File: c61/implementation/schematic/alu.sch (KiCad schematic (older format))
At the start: 22 parts, among them J4 CONN_02X05, U1 74LS32, U2 74LS32, U3 74LVC1G99, U30 EPM3064ATC44-ALU6, U4 74LVC1G99, U5 74LVC1G99, U6 74LVC1G99, U7 74LVC1G99, U8 74LVC1G99

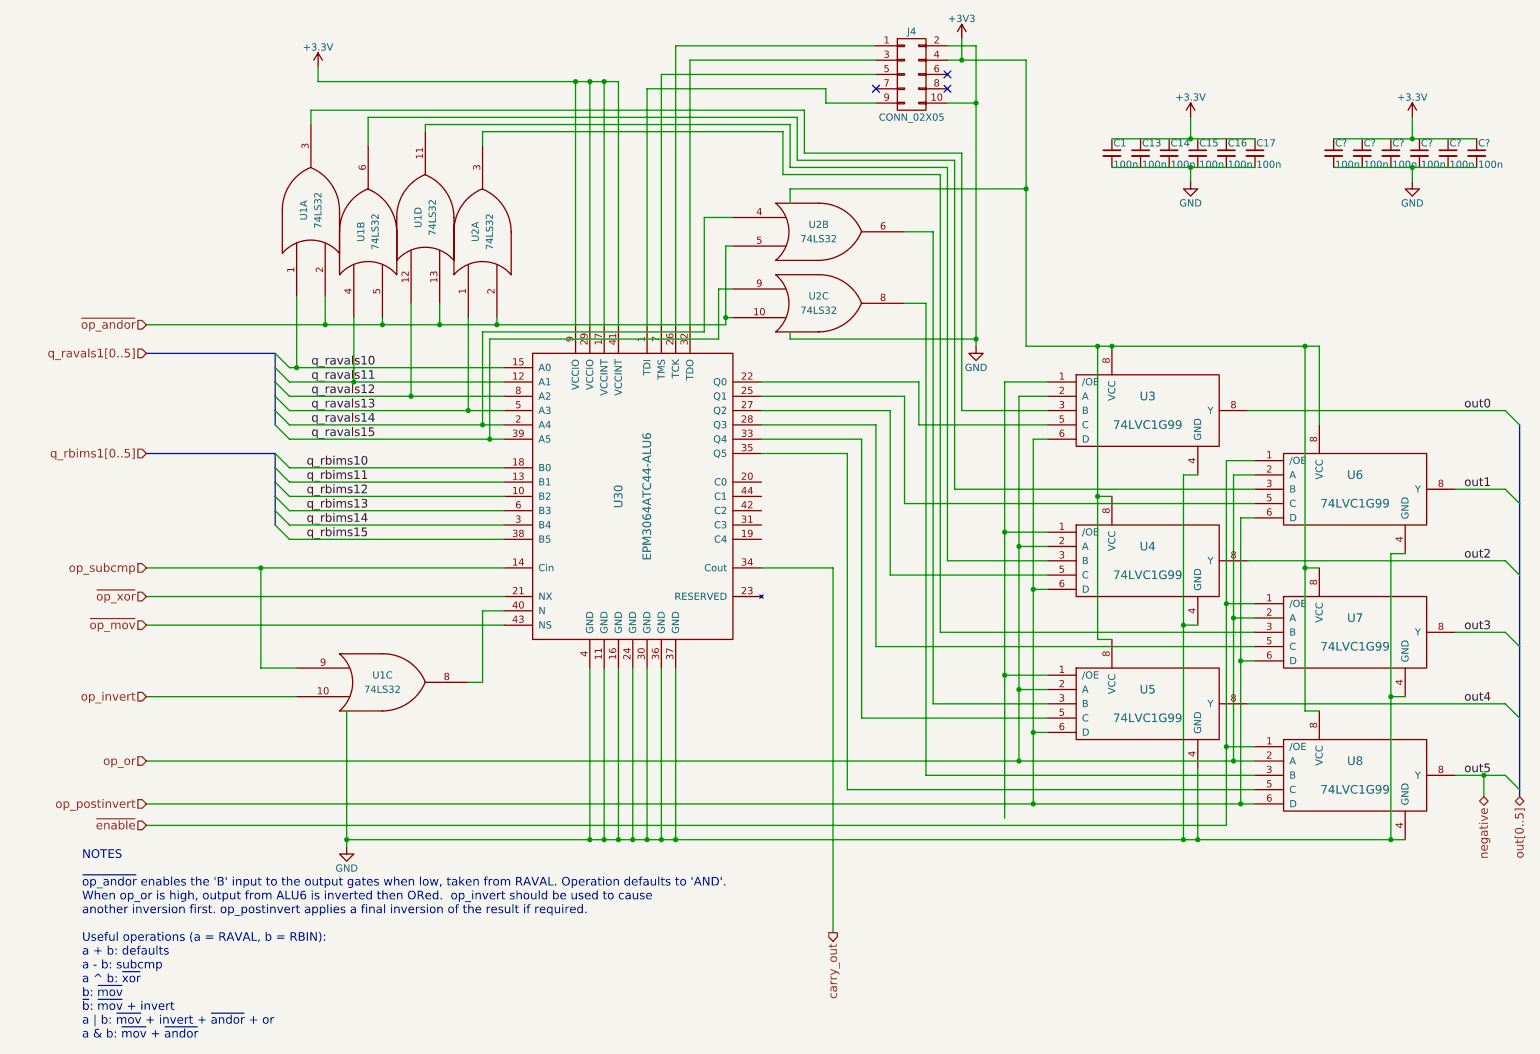
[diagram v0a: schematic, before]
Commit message: C61: more updates to schematic
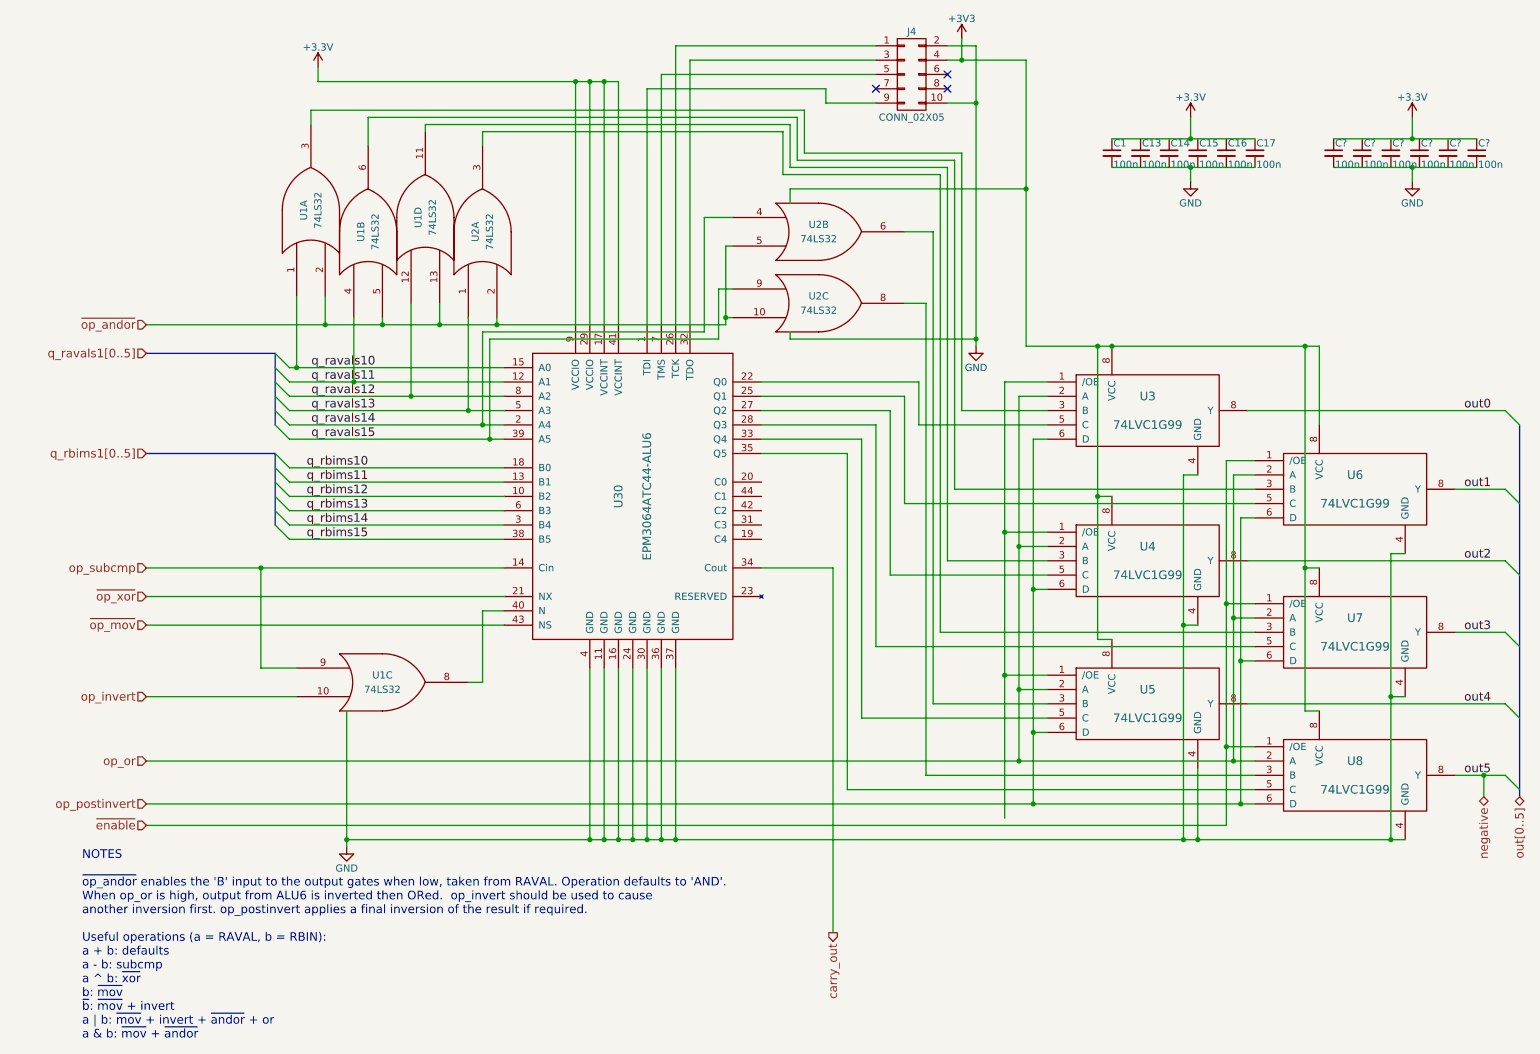
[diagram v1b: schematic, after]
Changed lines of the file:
@@
 $Descr A4 11693 8268
 encoding utf-8
-Sheet 7 8
+Sheet 7 9
 Title ""
 Date ""
@@
 	1400 3650 2300 3650
 Wire Bus Line
-	2300 3650 2300 3750
-Wire Bus Line
-	2300 3750 2300 3850
-Wire Bus Line
-	2300 3850 2300 3950
-Wire Bus Line
-	2300 3950 2300 4050
-Wire Bus Line
-	2300 4050 2300 4150
+	2300 3650 2300 4150
 Wire Wire Line
 	2400 3750 3900 3750
@@
 	1400 2950 2300 2950
 Wire Bus Line
-	2300 2950 2300 3050
-Wire Bus Line
-	2300 3050 2300 3150
-Wire Bus Line
-	2300 3150 2300 3250
-Wire Bus Line
-	2300 3250 2300 3350
-Wire Bus Line
-	2300 3350 2300 3450
-Wire Wire Line
-	2400 3050 2450 3050
-Wire Wire Line
-	2450 3050 3900 3050
-Wire Wire Line
-	2400 3150 2850 3150
-Wire Wire Line
-	2850 3150 3900 3150
-Wire Wire Line
-	2400 3250 3250 3250
-Wire Wire Line
-	3250 3250 3900 3250
-Wire Wire Line
-	2400 3350 3650 3350
-Wire Wire Line
-	3650 3350 3900 3350
-Wire Wire Line
-	2400 3450 3750 3450
-Wire Wire Line
-	3750 3450 3900 3450
-Wire Wire Line
-	2400 3550 3800 3550
-Wire Wire Line
-	3800 3550 3900 3550
-Wire Wire Line
-	1400 4450 2200 4450
-Wire Wire Line
-	2200 4450 3900 4450
+	2300 2950 2300 3450
+Wire Wire Line
+	2400 3050 3900 3050
+Wire Wire Line
+	2400 3150 3900 3150
+Wire Wire Line
+	2400 3250 3900 3250
+Wire Wire Line
+	2400 3350 3900 3350
+Wire Wire Line
+	2400 3450 3900 3450
+Wire Wire Line
+	2400 3550 3900 3550
+Wire Wire Line
+	1400 4450 3900 4450
 Wire Wire Line
 	1400 4650 3900 4650
@@
 	1400 5350 2450 5350
 Wire Wire Line
-	2800 5450 2800 6350
-Wire Wire Line
-	2800 6350 2800 6400
-Wire Wire Line
-	2800 6350 4500 6350
-Wire Wire Line
-	4500 6350 4600 6350
-Wire Wire Line
-	4600 6350 4700 6350
-Wire Wire Line
-	4700 6350 4800 6350
-Wire Wire Line
-	4800 6350 4900 6350
-Wire Wire Line
-	4900 6350 5000 6350
-Wire Wire Line
-	5000 6350 5100 6350
-Wire Wire Line
-	5100 6350 8650 6350
-Wire Wire Line
-	8650 6350 8750 6350
-Wire Wire Line
-	8750 6350 10100 6350
-Wire Wire Line
-	10100 6350 10200 6350
+	2800 5450 2800 6400
+Wire Wire Line
+	2800 6350 10200 6350
 Wire Wire Line
 	5100 6350 5100 5150
@@
 	2600 950  2600 1050
 Wire Wire Line
-	2600 1050 4400 1050
-Wire Wire Line
-	4400 1050 4500 1050
-Wire Wire Line
-	4500 1050 4600 1050
-Wire Wire Line
-	4600 1050 4700 1050
+	2600 1050 4700 1050
 Wire Wire Line
 	4700 1050 4700 2750
@@
 	7000 800  7200 800
 Wire Wire Line
-	7200 800  7200 1200
-Wire Wire Line
-	7200 1200 7200 2850
-Wire Wire Line
-	7200 2850 7200 2900
+	7200 800  7200 2900
 Wire Wire Line
 	7000 1200 7200 1200
 Connection ~ 7200 1200
 Wire Wire Line
-	7000 900  7100 900
-Wire Wire Line
-	7100 900  7550 900
+	7000 900  7550 900
 Wire Wire Line
 	7100 900  7100 750
@@
 	8700 1300 8700 1450
 Wire Wire Line
-	8150 1450 8700 1450
-Wire Wire Line
-	8700 1450 9150 1450
+	8150 1450 9150 1450
 Connection ~ 8700 1450
 Wire Wire Line
-	8150 1650 8700 1650
-Wire Wire Line
-	8700 1650 9150 1650
+	8150 1650 9150 1650
 Wire Wire Line
 	8700 1650 8700 1750
@@
 Connection ~ 2450 3050
 Wire Wire Line
-	5450 2750 3850 2750
-Wire Wire Line
-	3850 2750 3450 2750
-Wire Wire Line
-	3450 2750 3050 2750
-Wire Wire Line
-	3050 2750 2650 2750
-Wire Wire Line
-	2650 2750 1400 2750
+	5450 2750 1400 2750
 Wire Wire Line
 	2650 2550 2650 2750
@@
 Connection ~ 3450 2750
 Wire Wire Line
-	5450 2200 5450 2700
-Wire Wire Line
-	5450 2700 5450 2750
+	5450 2200 5450 2750
 Wire Wire Line
 	5450 2700 5500 2700
@@
 Connection ~ 2200 4450
 Wire Wire Line
-	1400 6100 7600 6100
-Wire Wire Line
-	7600 6100 9050 6100
-Wire Wire Line
-	9050 6100 9150 6100
-Wire Wire Line
-	9050 4100 9050 5100
-Wire Wire Line
-	9050 5100 9050 6100
+	1400 6100 9150 6100
+Wire Wire Line
+	9050 4100 9050 6100
 Wire Wire Line
 	9050 5100 9150 5100
@@
 Connection ~ 9050 5100
 Wire Wire Line
-	7600 3550 7600 4600
-Wire Wire Line
-	7600 4600 7600 5600
-Wire Wire Line
-	7600 5600 7600 6100
+	7600 3550 7600 6100
 Wire Wire Line
 	7600 5600 7700 5600
@@
 Connection ~ 7600 4600
 Wire Wire Line
-	1400 5800 7500 5800
-Wire Wire Line
-	7500 5800 9000 5800
-Wire Wire Line
-	9000 5800 9150 5800
-Wire Wire Line
-	7500 3250 7500 4300
-Wire Wire Line
-	7500 4300 7500 5300
-Wire Wire Line
-	7500 5300 7500 5800
+	1400 5800 9150 5800
+Wire Wire Line
+	7500 3250 7500 5800
 Wire Wire Line
 	7500 5300 7700 5300
@@
 Connection ~ 7500 4300
 Wire Wire Line
-	9000 3800 9000 4800
-Wire Wire Line
-	9000 4800 9000 5800
+	9000 3800 9000 5800
 Wire Wire Line
 	9000 4800 9150 4800
@@
 	8950 5700 9150 5700
 Wire Wire Line
-	8950 3700 8950 4700
-Wire Wire Line
-	8950 4700 8950 5700
-Wire Wire Line
-	8950 5700 8950 6250
+	8950 3700 8950 6250
 Wire Wire Line
 	8950 6250 1400 6250
@@
 Connection ~ 8950 4700
 Wire Wire Line
-	7400 3150 7400 4200
-Wire Wire Line
-	7400 4200 7400 5200
-Wire Wire Line
-	7400 5200 7400 6200
+	7400 3150 7400 6200
 Wire Wire Line
 	7400 5200 7700 5200
@@
 Connection ~ 8750 6350
 Wire Wire Line
-	10100 4350 10100 5350
-Wire Wire Line
-	10100 5350 10100 6350
+	10100 4350 10100 6350
 Wire Wire Line
 	10100 5350 10200 5350
@@
 Connection ~ 10100 5350
 Wire Wire Line
-	8650 3800 8650 4850
-Wire Wire Line
-	8650 4850 8650 6350
+	8650 3800 8650 6350
 Wire Wire Line
 	8650 4850 8750 4850
@@
 Connection ~ 8650 4850
 Wire Wire Line
-	7550 900  7550 1800
-Wire Wire Line
-	7550 1800 7550 2900
-Wire Wire Line
-	7550 2900 8050 2900
-Wire Wire Line
-	8050 2900 8150 2900
-Wire Wire Line
-	8150 2900 9500 2900
-Wire Wire Line
-	9500 2900 9600 2900
+	7550 900  7550 2900
+Wire Wire Line
+	7550 2900 9600 2900
 Connection ~ 7100 900
 Wire Wire Line
-	8050 2900 8050 3950
-Wire Wire Line
-	8050 3950 8050 4950
+	8050 2900 8050 4950
 Wire Wire Line
 	8050 3950 8150 3950
@@
 Connection ~ 8150 2900
 Wire Wire Line
-	9500 2900 9500 4450
-Wire Wire Line
-	9500 4450 9500 5450
+	9500 2900 9500 5450
 Wire Wire Line
 	9500 4450 9600 4450
@@
 	10900 5900 11000 6000
 Wire Bus Line
-	11000 6050 11000 6000
-Wire Bus Line
-	11000 6000 11000 5500
-Wire Bus Line
-	11000 5500 11000 5000
-Wire Bus Line
-	11000 5000 11000 4500
-Wire Bus Line
-	11000 4500 11000 4000
-Wire Bus Line
-	11000 4000 11000 3450
+	11000 3450 11000 6050
 Entry Wire Line
 	10900 3350 11000 3450
@@
 	9100 5400 10900 5400
 Wire Wire Line
-	10550 5900 10750 5900
-Wire Wire Line
-	10750 5900 10900 5900
+	10550 5900 10900 5900
 Text HLabel 10750 6050 3    60   3State ~ 0
 negative
@@
 	10250 1300 10250 1450
 Wire Wire Line
-	9700 1450 10250 1450
-Wire Wire Line
-	10250 1450 10700 1450
+	9700 1450 10700 1450
 Connection ~ 10250 1450
 Wire Wire Line
-	9700 1650 10250 1650
-Wire Wire Line
-	10250 1650 10700 1650
+	9700 1650 10700 1650
 Wire Wire Line
 	10250 1650 10250 1750
